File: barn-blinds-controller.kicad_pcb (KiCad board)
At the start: 4 copper layers, 65 x 60 mm, 69 parts, among them J1 DC005-T25, J2 KH-TYPE-C-16P (Kinghelm), J3 Conn_01x08, SW1 RESET, SW2 BOOT, U1 DCDC Converter, U10 TMP235, U11 ACS723xLCTR-05AB, U2 AP2112K-3.3, U3 ESP32-S3-WROOM-1, U4 ISO7760DBQ, U5 ISO7760DBQ, U6 ISO7760DBQ, U7 AMS1117-3.3, U8 TB6612FNG, U9 TB6612FNG

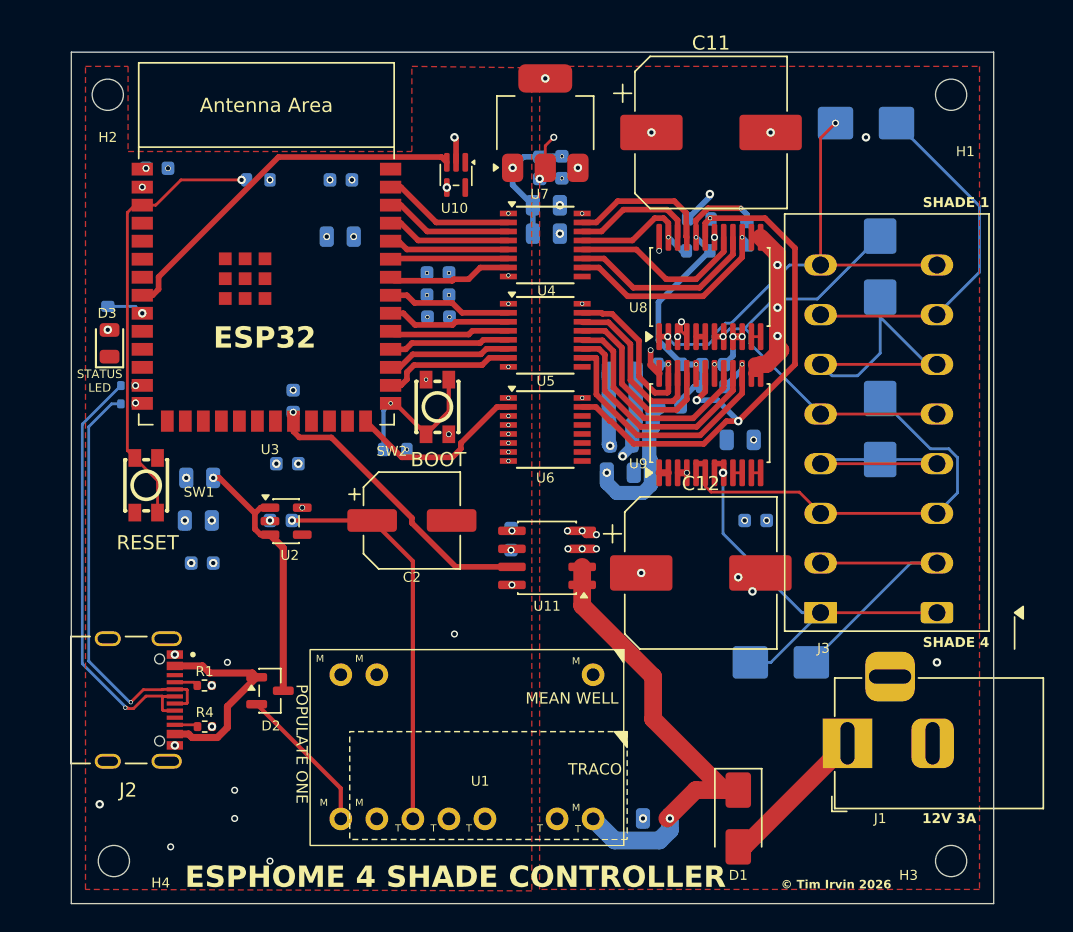
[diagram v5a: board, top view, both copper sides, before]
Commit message: Replaced fuses and rearranged to fit better
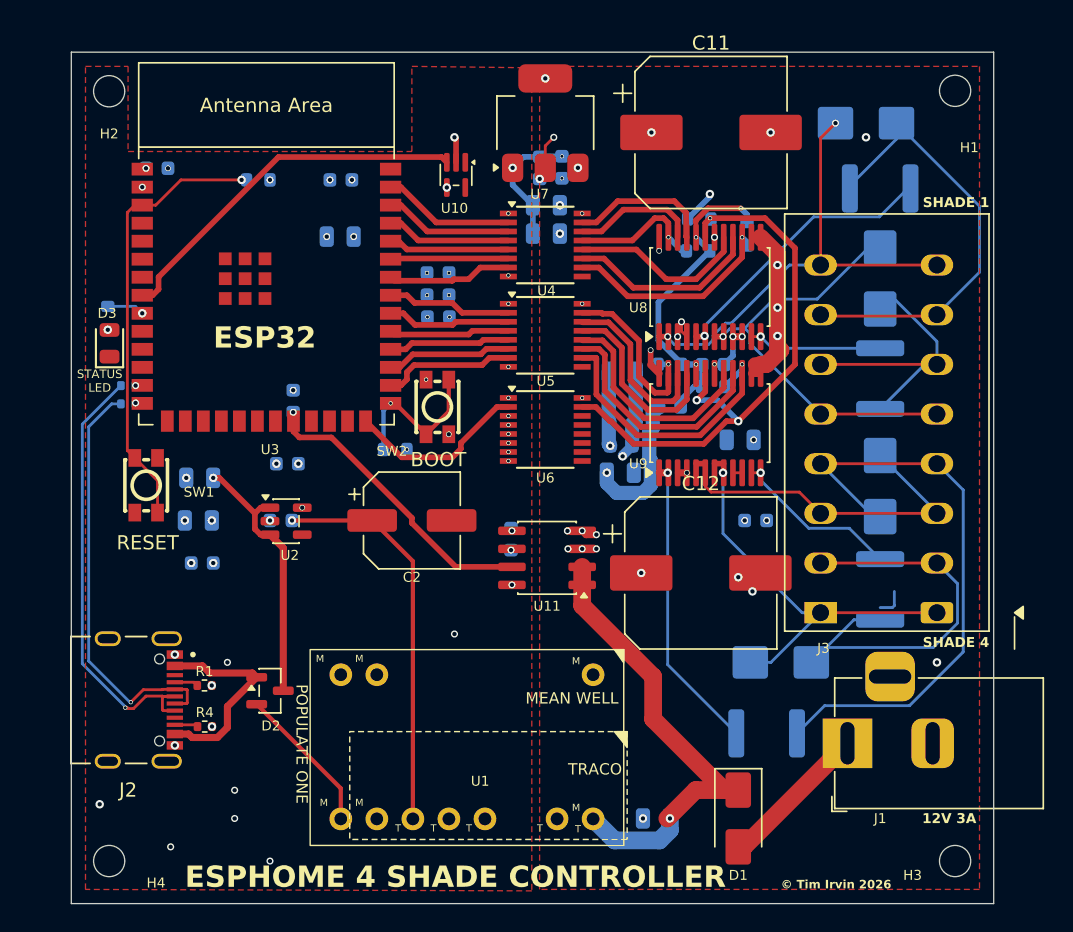
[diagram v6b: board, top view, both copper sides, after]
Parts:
- added F1: Polyfuse mSMD110, Fuse:Fuse_1812_4532Metric, B.Cu at (134.0, 58.6)
- added F2: Polyfuse mSMD110, Fuse:Fuse_1812_4532Metric, B.Cu at (134.0, 86.9)
- added F3: Polyfuse mSMD110, Fuse:Fuse_1812_4532Metric, B.Cu at (134.0, 72.0)
- added F4: Polyfuse mSMD110, Fuse:Fuse_1812_4532Metric, B.Cu at (126.0, 97.0)
- C1: value 22uF -> 22uF 25V
- C5: value 22uF -> 22uF 10V
- moved D7 4.02 mm to (134.0, 79.6)
- moved D6 0.84 mm to (134.0, 64.9)
- moved H1 0.39 mm to (139.3, 51.7)
- moved H4 0.33 mm to (79.7, 106.0)
- moved H3 0.28 mm to (139.3, 106.0)
- moved H2 0.27 mm to (79.7, 51.8)
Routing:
- net Net-(J3-Pin_4): track 15.8 -> 42.1 mm
- net U3_A01: track 0.65 -> 21.0 mm, vias 0 -> 1
- net U2_A02: track 0.65 -> 20.0 mm, vias 0 -> 1
- net U3_B01: track 0.65 -> 11.9 mm, vias 0 -> 1
- net Net-(J3-Pin_2): track 19.9 -> 30.6 mm
- net U2_B01: track 0.65 -> 9.41 mm, vias 0 -> 1
- net U3_A02: track 30.4 -> 24.4 mm
- net Net-(J3-Pin_7): track 25.2 -> 30.9 mm
- net Net-(J3-Pin_6): track 23.5 -> 20.3 mm
- net (no net): track 0.00 -> 2.06 mm

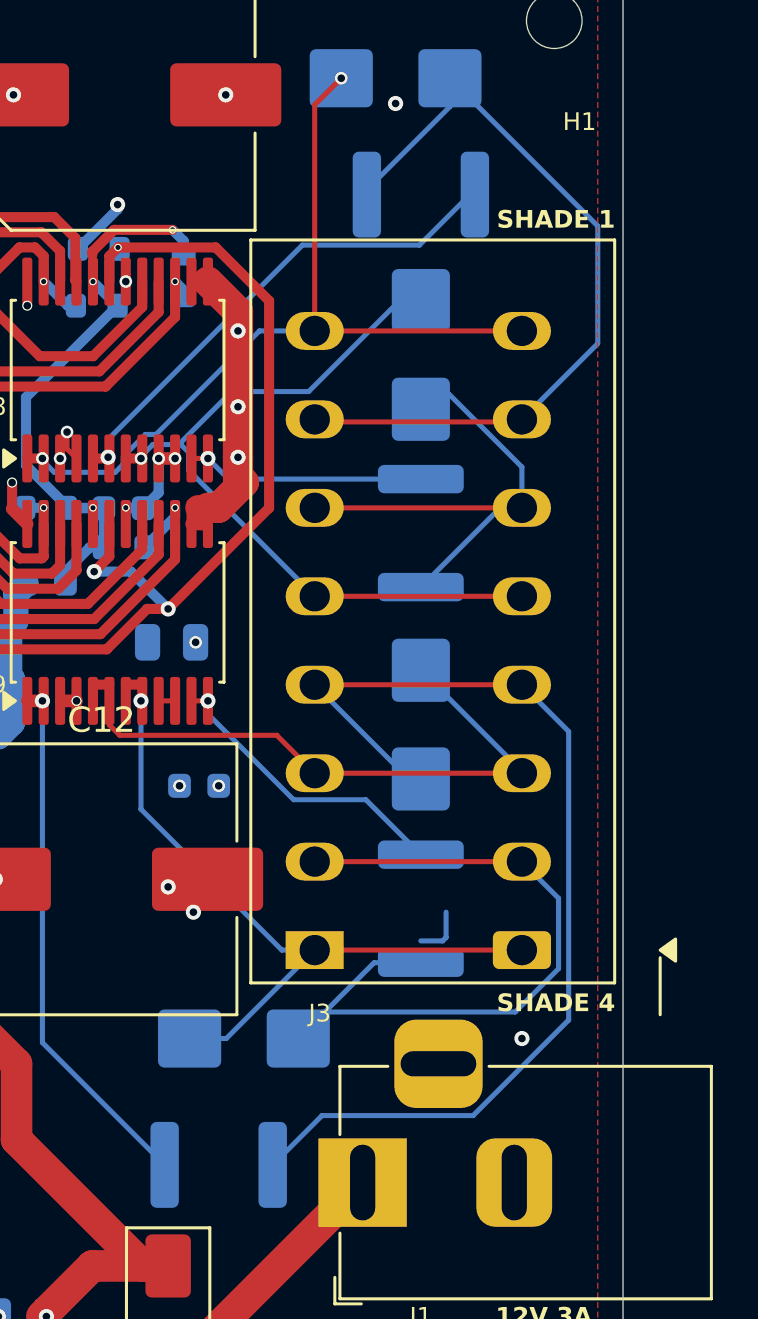
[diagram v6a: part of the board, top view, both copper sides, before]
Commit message: Updated connector to match actual footprint, updated 3D images.
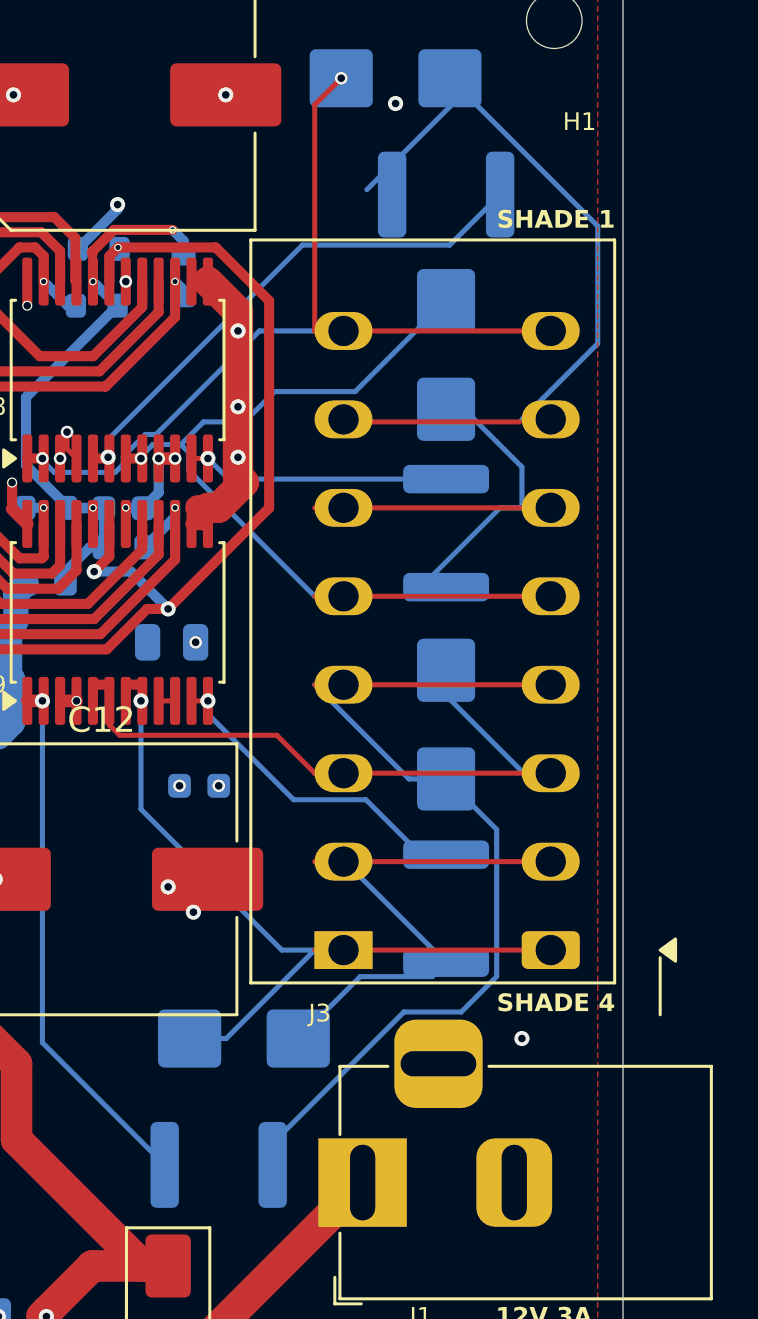
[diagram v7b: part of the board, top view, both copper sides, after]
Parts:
- moved D6 1.00 mm to (135.0, 64.9)
- moved D7 1.00 mm to (135.0, 79.6)
- moved F1 1.00 mm to (135.0, 58.6)
- moved F2 1.00 mm to (135.0, 86.9)
- moved F3 1.00 mm to (135.0, 72.0)
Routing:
- net Net-(J3-Pin_2): track 30.6 -> 21.0 mm
- net Net-(J3-Pin_4): track 42.1 -> 35.0 mm
- net (no net): track 2.06 -> 0.00 mm
- net U2_A02: track 20.0 -> 20.9 mm
- net U2_B02: track 31.2 -> 31.8 mm
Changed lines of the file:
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@@
 		)
 		(pad "1" thru_hole rect
-			(at 0 -8.2 90)
+			(at 0 -7.06 90)
 			(size 1.5 2.3)
 			(drill 1.2)
@@
 		)
 		(pad "1" thru_hole roundrect
-			(at 0 0 90)
+			(at 0 1.14 90)
 			(size 1.5 2.3)
 			(drill 1.2)
@@
 		)
 		(pad "2" thru_hole oval
-			(at 3.5 -8.2 90)
+			(at 3.5 -7.06 90)
 			(size 1.5 2.3)
 			(drill 1.2)
@@
 		)
 		(pad "2" thru_hole oval
-			(at 3.5 0 90)
+			(at 3.5 1.14 90)
 			(size 1.5 2.3)
 			(drill 1.2)
@@
 		)
 		(pad "3" thru_hole oval
-			(at 7 -8.2 90)
+			(at 7 -7.06 90)
 			(size 1.5 2.3)
 			(drill 1.2)
@@
 		)
 		(pad "3" thru_hole oval
-			(at 7 0 90)
+			(at 7 1.14 90)
 			(size 1.5 2.3)
 			(drill 1.2)
@@
 		)
 		(pad "4" thru_hole oval
-			(at 10.5 -8.2 90)
+			(at 10.5 -7.06 90)
 			(size 1.5 2.3)
 			(drill 1.2)
@@
 		)
 		(pad "4" thru_hole oval
-			(at 10.5 0 90)
+			(at 10.5 1.14 90)
 			(size 1.5 2.3)
 			(drill 1.2)
@@
 		)
 		(pad "5" thru_hole oval
-			(at 14 -8.2 90)
+			(at 14 -7.06 90)
 			(size 1.5 2.3)
 			(drill 1.2)
@@
 		)
 		(pad "5" thru_hole oval
-			(at 14 0 90)
+			(at 14 1.14 90)
 			(size 1.5 2.3)
 			(drill 1.2)
@@
 		)
 		(pad "6" thru_hole oval
-			(at 17.5 -8.2 90)
+			(at 17.5 -7.06 90)
 			(size 1.5 2.3)
 			(drill 1.2)
@@
 		)
 		(pad "6" thru_hole oval
-			(at 17.5 0 90)
+			(at 17.5 1.14 90)
 			(size 1.5 2.3)
 			(drill 1.2)
@@
 		)
 		(pad "7" thru_hole oval
-			(at 21 -8.2 90)
+			(at 21 -7.06 90)
 			(size 1.5 2.3)
 			(drill 1.2)
@@
 		)
 		(pad "7" thru_hole oval
-			(at 21 0 90)
+			(at 21 1.14 90)
 			(size 1.5 2.3)
 			(drill 1.2)
@@
 		)
 		(pad "8" thru_hole oval
-			(at 24.5 -8.2 90)
+			(at 24.5 -7.06 90)
 			(size 1.5 2.3)
 			(drill 1.2)
@@
 		)
 		(pad "8" thru_hole oval
-			(at 24.5 0 90)
+			(at 24.5 1.14 90)
 			(size 1.5 2.3)
 			(drill 1.2)
@@
 		)
 		(embedded_fonts no)
-		(model "${KICAD9_3DMODEL_DIR}/TerminalBlock_WAGO.3dshapes/TerminalBlock_WAGO_2601-1108_1x08_P3.50mm_Horizontal.step"
+		(model "${KIPRJMOD}/JL217R-35008G01-BodyPad001.step"
 			(offset
-				(xyz 0 0 0)
+				(xyz 10.25 5.4 0)
 			)
 			(scale
@@
 			)
 			(rotate
-				(xyz 0 0 0)
+				(xyz -0 -0 -0)
 			)
 		)
@@
 	(footprint "Fuse:Fuse_1812_4532Metric"
 		(layer "B.Cu")
-		(at 134 72 -90)
+		(at 135 72 -90)
 		(descr "Fuse SMD 1812 (4532 Metric), square (rectangular) end terminal, IPC-7351 nominal, (Body size source: https://www.nikhef.nl/pub/departments/mt/projects/detectorR_D/dtddice/ERJ2G.pdf), generated with kicad-footprint-generator")
 		(tags "fuse")
@@
 	(footprint "Fuse:Fuse_1812_4532Metric"
 		(layer "B.Cu")
-		(at 134 86.8625 -90)
+		(at 135 86.8625 -90)
 		(descr "Fuse SMD 1812 (4532 Metric), square (rectangular) end terminal, IPC-7351 nominal, (Body size source: https://www.nikhef.nl/pub/departments/mt/projects/detectorR_D/dtddice/ERJ2G.pdf), generated with kicad-footprint-generator")
 		(tags "fuse")
@@
 	(footprint "PCM_JLCPCB:D_SMB"
 		(layer "B.Cu")
-		(at 134 79.577895 -90)
+		(at 135 79.577895 -90)
 		(descr "Diode SMB (DO-214AA)")
 		(tags "Diode SMB (DO-214AA)")
@@
 	(footprint "PCM_JLCPCB:D_SMB"
 		(layer "B.Cu")
-		(at 134 64.948684 -90)
+		(at 135 64.948684 -90)
 		(descr "Diode SMB (DO-214AA)")
 		(tags "Diode SMB (DO-214AA)")
@@
 	(footprint "Fuse:Fuse_1812_4532Metric"
 		(layer "B.Cu")
-		(at 134 58.604079 180)
+		(at 135 58.604079 180)
 		(descr "Fuse SMD 1812 (4532 Metric), square (rectangular) end terminal, IPC-7351 nominal, (Body size source: https://www.nikhef.nl/pub/departments/mt/projects/detectorR_D/dtddice/ERJ2G.pdf), generated with kicad-footprint-generator")
 		(tags "fuse")
@@
 	)
 	(segment
-		(start 135 88)
-		(end 134.8625 88.1375)
-		(width 0.2)
-		(layer "B.Cu")
-		(net 0)
-	)
-	(segment
-		(start 134.8625 88.1375)
-		(end 134 88.1375)
-		(width 0.2)
-		(layer "B.Cu")
-		(net 0)
-	)
-	(segment
-		(start 135 87)
-		(end 135 88)
-		(width 0.2)
-		(layer "B.Cu")
-		(net 0)
-	)
-	(segment
 		(start 126.99595 69.99595)
 		(end 126.764525 69.764525)
@@
 	)
 	(segment
-		(start 129.311917 60.604079)
-		(end 121.625 68.290996)
+		(start 135.1375 60.604079)
+		(end 129.311917 60.604079)
 		(width 0.2)
 		(layer "B.Cu")
@@
 	)
 	(segment
-		(start 136.1375 58.411428)
-		(end 133.944849 60.604079)
+		(start 137.1375 58.604079)
+		(end 135.1375 60.604079)
 		(width 0.2)
 		(layer "B.Cu")
@@
 	)
 	(segment
-		(start 133.944849 60.604079)
-		(end 129.311917 60.604079)
+		(start 121.625 68.290996)
+		(end 121.625 68.99595)
 		(width 0.2)
 		(layer "B.Cu")
@@
 	)
 	(segment
-		(start 121.625 68.290996)
-		(end 121.625 68.99595)
+		(start 129.311917 60.604079)
+		(end 121.625 68.290996)
 		(width 0.2)
 		(layer "B.Cu")
@@
 	)
 	(segment
-		(start 126.515996 66.4)
-		(end 124.502818 68.413178)
+		(start 135 62.798684)
+		(end 131.398684 66.4)
 		(width 0.2)
 		(layer "B.Cu")
@@
 	)
 	(segment
-		(start 124.502818 68.413178)
-		(end 124.502818 68.49595)
+		(start 123.397182 68.49595)
+		(end 122.925 68.968132)
 		(width 0.2)
 		(layer "B.Cu")
@@
 	)
 	(segment
-		(start 123.397182 68.49595)
-		(end 122.925 68.968132)
+		(start 131.398684 66.4)
+		(end 128.213054 66.4)
+		(width 0.2)
+		(layer "B.Cu")
+		(net 14)
+	)
+	(segment
+		(start 125.398768 67.6)
+		(end 124.502818 68.49595)
 		(width 0.2)
 		(layer "B.Cu")
@@
 	)
 	(segment
-		(start 134 61.961686)
-		(end 129.561686 66.4)
+		(start 127.013054 67.6)
+		(end 125.398768 67.6)
 		(width 0.2)
 		(layer "B.Cu")
@@
 	)
 	(segment
-		(start 129.561686 66.4)
-		(end 126.515996 66.4)
+		(start 128.213054 66.4)
+		(end 127.013054 67.6)
 		(width 0.2)
 		(layer "B.Cu")
@@
 	)
 	(segment
-		(start 139.45 86.45)
-		(end 139.45 89.234744)
-		(width 0.2)
-		(layer "B.Cu")
-		(net 26)
-	)
-	(segment
-		(start 130.2 90.95)
+		(start 131.6 89.55)
 		(end 129.15 92)
 		(width 0.2)
@@
 	)
 	(segment
-		(start 138 85)
-		(end 139.45 86.45)
-		(width 0.2)
-		(layer "B.Cu")
-		(net 26)
-	)
-	(segment
-		(start 132.15 89)
-		(end 129.15 92)
+		(start 134.45 89.55)
+		(end 131.6 89.55)
 		(width 0.2)
 		(layer "B.Cu")
@@
 	)
 	(segment
-		(start 139.45 89.234744)
-		(end 137.734744 90.95)
+		(start 130.94 85)
+		(end 131 85)
 		(width 0.2)
 		(layer "B.Cu")
@@
 	)
 	(segment
-		(start 134 89)
-		(end 132.15 89)
+		(start 131 85)
+		(end 135 89)
 		(width 0.2)
 		(layer "B.Cu")
@@
 	)
 	(segment
-		(start 137.734744 90.95)
-		(end 130.2 90.95)
+		(start 135 89)
+		(end 134.45 89.55)
 		(width 0.2)
 		(layer "B.Cu")
@@
 	)
 	(segment
-		(start 128.1375 97)
-		(end 130.0875 95.05)
+		(start 135.597244 90.95)
+		(end 137 89.547244)
 		(width 0.2)
 		(layer "B.Cu")
@@
 	)
 	(segment
-		(start 139.85 91.265896)
-		(end 139.85 79.85)
+		(start 133.3279 90.95)
+		(end 135.597244 90.95)
 		(width 0.2)
 		(layer "B.Cu")
@@
 	)
 	(segment
-		(start 139.85 79.85)
-		(end 138 78)
+		(start 137 89.547244)
+		(end 137 83.727895)
 		(width 0.2)
 		(layer "B.Cu")
@@
 	)
 	(segment
-		(start 130.0875 95.05)
-		(end 136.065896 95.05)
+		(start 128.1375 97)
+		(end 128.1375 96.1404)
 		(width 0.2)
 		(layer "B.Cu")
@@
 	)
 	(segment
-		(start 136.065896 95.05)
-		(end 139.85 91.265896)
+		(start 137 83.727895)
+		(end 135 81.727895)
+		(width 0.2)
+		(layer "B.Cu")
+		(net 35)
+	)
+	(segment
+		(start 128.1375 96.1404)
+		(end 133.3279 90.95)
 		(width 0.2)
 		(layer "B.Cu")

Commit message: Final cleanup
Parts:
- H1, H2, H3, H4: footprint MountingHole:MountingHole_2.2mm_M2 -> MountingHole:MountingHole_3.2mm_M3
- R2, R3: moved to F.Cu
- moved C_ISO_A1 8.01 mm to (107.8, 74.0), turned to 90 degrees
- moved C2 6.69 mm to (96.5, 86.9)
- moved C_ACS1 6.40 mm to (88.8, 60.0)
- moved C_ISO_E1 6.17 mm to (107.0, 60.0)
- moved SW2 5.40 mm to (102.6, 79.4)
- moved C3 5.31 mm to (90.0, 87.0)
- moved R_BOOT1 4.53 mm to (104.3, 77.4)
- moved C5 4.14 mm to (90.0, 81.1)
- moved C_ISO_C1 4.13 mm to (107.0, 66.5)
- moved C4 4.07 mm to (90.0, 78.0)
- moved C6 3.91 mm to (90.0, 84.0)
- moved U2 3.81 mm to (95.7, 80.7)
- moved C8 3.36 mm to (98.7, 60.0)
- moved C_ACS2 3.32 mm to (95.9, 73.9)
- moved U3 3.25 mm to (94.0, 65.5)
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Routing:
- net +5V_ISO: track 45.1 -> 28.4 mm, vias 1 -> 2
- net +3.3V_MOTOR: track 25.1 -> 39.4 mm, vias 13 -> 10
- net /ISO_STBY: track 12.8 -> 23.6 mm
- net GND_ISO: track 1.81 -> 11.4 mm, vias 35 -> 39
- net +5V_OR: track 18.9 -> 23.0 mm
- net /ISO_PWM_M4: track 9.40 -> 5.85 mm
- net /ISO_M3_CLOSE: track 8.73 -> 5.30 mm
- net /ISO_M1_CLOSE: track 9.07 -> 5.82 mm
- net /ISO_PWM_M3: track 8.81 -> 5.56 mm
- net /ISO_PWM_M1: track 8.81 -> 5.56 mm
- net /ISO_M4_OPEN: track 8.58 -> 5.33 mm
- net /ISO_M1_OPEN: track 9.33 -> 6.08 mm
- net /ISO_M4_CLOSE: track 8.84 -> 5.59 mm
- net /ISO_M2_OPEN: track 8.54 -> 5.29 mm
- net Net-(U3-GPIO16/U0CTS/ADC2_CH5/XTAL_32K_N): track 2.63 -> 5.88 mm
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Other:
- outline, holes or cut-outs redrawn
- board text removed: "12V 3A"
